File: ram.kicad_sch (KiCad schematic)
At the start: 7 parts, among them U1 LFE5U-85F-6BG381C, U2 IS42S16160J-6TL

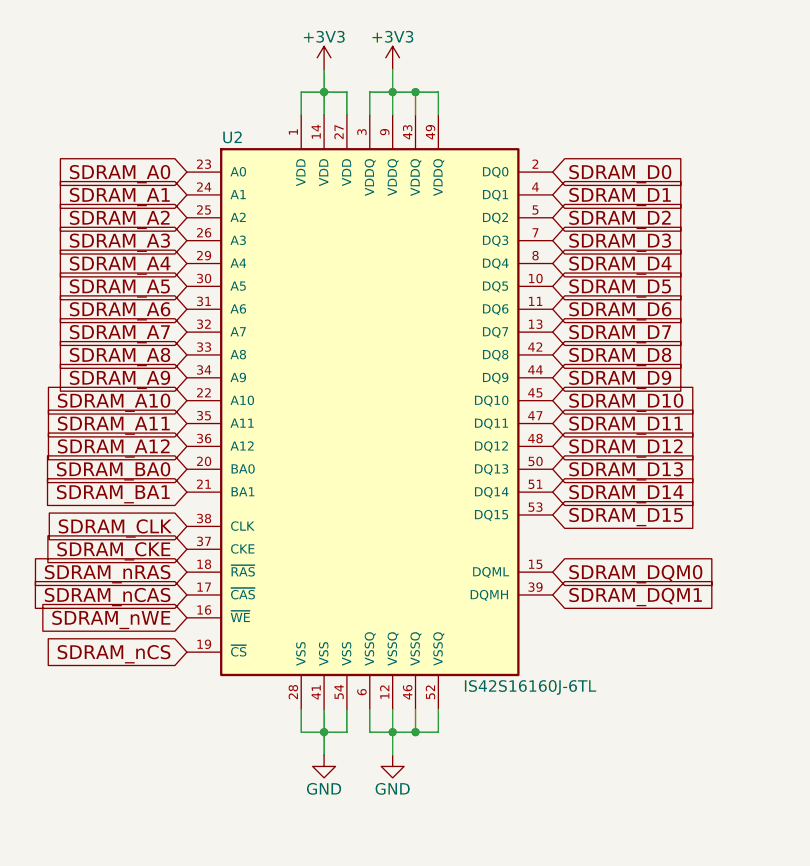
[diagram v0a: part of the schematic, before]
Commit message: update schematic with new footprint for ram. pre-wiring the ram on pcb
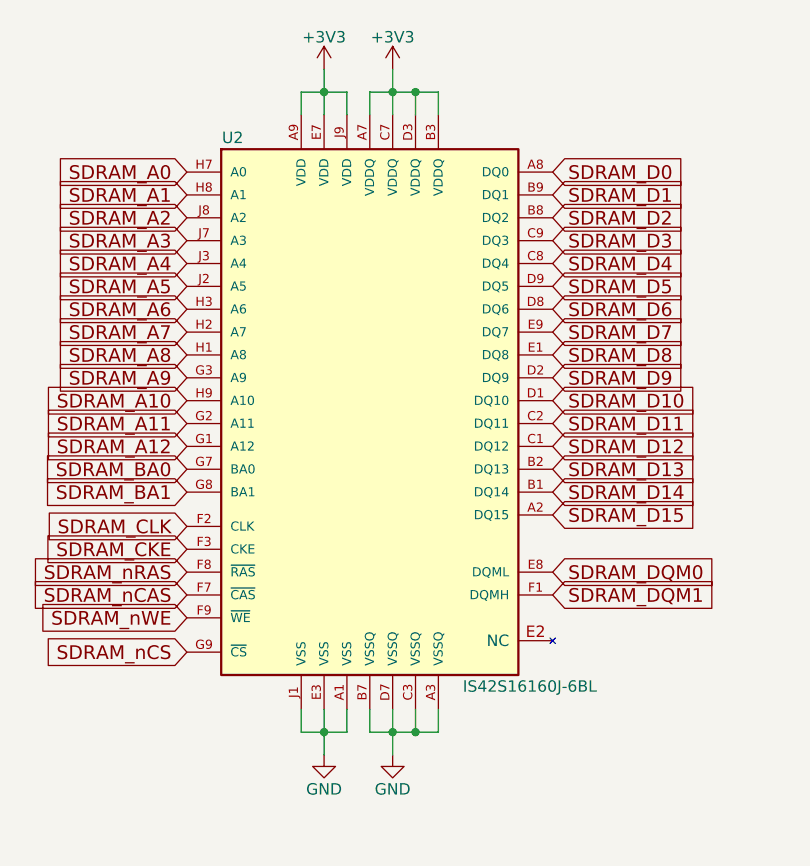
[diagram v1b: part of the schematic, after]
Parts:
- U2: value IS42S16160J-6TL -> IS42S16160J-6BL; footprint TSOP54:TSOP54 -> sdram:BGA54C80P9X9_800X800X120; symbol mt48lc16m16a2tg:MT48LC16M16A2TG -> mt48lc16m16a2tg:MT48LC16M16A2TG_BGA; MPN 870-IS42S16160J-6TL -> 870-42S16160J6BL
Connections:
- net +3V3: now also U2.A7 (VDDQ), U2.A9 (VDD), U2.B3 (VDDQ), U2.C7 (VDDQ), U2.D3 (VDDQ), U2.E7 (VDD), U2.J9 (VDD); no longer U2.1 (VDD), U2.14 (VDD), U2.27 (VDD), U2.3 (VDDQ), U2.43 (VDDQ), U2.49 (VDDQ), U2.9 (VDDQ)
- net GND: now also U2.A1 (VSS), U2.A3 (VSSQ), U2.B7 (VSSQ), U2.C3 (VSSQ), U2.D7 (VSSQ), U2.E3 (VSS), U2.J1 (VSS); no longer U2.12 (VSSQ), U2.28 (VSS), U2.41 (VSS), U2.46 (VSSQ), U2.52 (VSSQ), U2.54 (VSS), U2.6 (VSSQ)
- net SDRAM_A0: now also U2.H7 (A0); no longer U2.23 (A0)
- net SDRAM_A1: now also U2.H8 (A1); no longer U2.24 (A1)
- net SDRAM_A10: now also U2.H9 (A10); no longer U2.22 (A10)
- net SDRAM_A11: now also U2.G2 (A11); no longer U2.35 (A11)
- net SDRAM_A12: now also U2.G1 (A12); no longer U2.36 (A12)
- net SDRAM_A2: now also U2.J8 (A2); no longer U2.25 (A2)
- net SDRAM_A3: now also U2.J7 (A3); no longer U2.26 (A3)
- net SDRAM_A4: now also U2.J3 (A4); no longer U2.29 (A4)
- net SDRAM_A5: now also U2.J2 (A5); no longer U2.30 (A5)
- net SDRAM_A6: now also U2.H3 (A6); no longer U2.31 (A6)
- net SDRAM_A7: now also U2.H2 (A7); no longer U2.32 (A7)
- net SDRAM_A8: now also U2.H1 (A8); no longer U2.33 (A8)
- net SDRAM_A9: now also U2.G3 (A9); no longer U2.34 (A9)
- net SDRAM_BA0: now also U2.G7 (BA0); no longer U2.20 (BA0)
- net SDRAM_BA1: now also U2.G8 (BA1); no longer U2.21 (BA1)
- net SDRAM_CKE: now also U2.F3 (CKE); no longer U2.37 (CKE)
- net SDRAM_CLK: now also U2.F2 (CLK); no longer U2.38 (CLK)
- net SDRAM_D0: now also U2.A8 (DQ0); no longer U2.2 (DQ0)
- net SDRAM_D1: now also U2.B9 (DQ1); no longer U2.4 (DQ1)
- net SDRAM_D10: now also U2.D1 (DQ10); no longer U2.45 (DQ10)
- net SDRAM_D11: now also U2.C2 (DQ11); no longer U2.47 (DQ11)
- net SDRAM_D12: now also U2.C1 (DQ12); no longer U2.48 (DQ12)
- net SDRAM_D13: now also U2.B2 (DQ13); no longer U2.50 (DQ13)
- net SDRAM_D14: now also U2.B1 (DQ14); no longer U2.51 (DQ14)
- net SDRAM_D15: now also U2.A2 (DQ15); no longer U2.53 (DQ15)
- net SDRAM_D2: now also U2.B8 (DQ2); no longer U2.5 (DQ2)
- net SDRAM_D3: now also U2.C9 (DQ3); no longer U2.7 (DQ3)
- net SDRAM_D4: now also U2.C8 (DQ4); no longer U2.8 (DQ4)
- net SDRAM_D5: now also U2.D9 (DQ5); no longer U2.10 (DQ5)
- net SDRAM_D6: now also U2.D8 (DQ6); no longer U2.11 (DQ6)
- net SDRAM_D7: now also U2.E9 (DQ7); no longer U2.13 (DQ7)
- net SDRAM_D8: now also U2.E1 (DQ8); no longer U2.42 (DQ8)
- net SDRAM_D9: now also U2.D2 (DQ9); no longer U2.44 (DQ9)
- net SDRAM_DQM0: now also U2.E8 (DQML); no longer U2.15 (DQML)
- net SDRAM_DQM1: now also U2.F1 (DQMH); no longer U2.39 (DQMH)
- net SDRAM_nCAS: now also U2.F7 (~{CAS}); no longer U2.17 (~{CAS})
- net SDRAM_nCS: now also U2.G9 (~{CS}); no longer U2.19 (~{CS})
- net SDRAM_nRAS: now also U2.F8 (~{RAS}); no longer U2.18 (~{RAS})
- net SDRAM_nWE: now also U2.F9 (~{WE}); no longer U2.16 (~{WE})
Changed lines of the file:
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@@
 	)
 	(symbol
-		(lib_id "mt48lc16m16a2tg:MT48LC16M16A2TG")
+		(lib_id "mt48lc16m16a2tg:MT48LC16M16A2TG_BGA")
 		(at 138.43 88.9 0)
 		(unit 1)
@@
 			)
 		)
-		(property "Value" "IS42S16160J-6TL"
+		(property "Value" "IS42S16160J-6BL"
 			(at 156.21 119.38 0)
 			(show_name no)
@@
 			)
 		)
-		(property "Footprint" "TSOP54:TSOP54"
+		(property "Footprint" "sdram:BGA54C80P9X9_800X800X120"
 			(at 138.43 88.9 0)
 			(hide yes)
@@
 			)
 		)
-		(property "Description" ""
-			(at 138.43 88.9 0)
+		(property "Description" "SDRAM"
+			(at 138.43 88.9 0)
+			(hide yes)
 			(show_name no)
 			(do_not_autoplace no)
@@
 			)
 		)
-		(property "MPN" "870-IS42S16160J-6TL"
+		(property "MPN" "870-42S16160J6BL"
 			(at 138.43 88.9 0)
 			(hide yes)
@@
 			)
 		)
-		(pin "52"
-		)
-		(pin "2"
-		)
-		(pin "4"
-		)
-		(pin "5"
-		)
-		(pin "7"
-		)
-		(pin "8"
-		)
-		(pin "10"
-		)
-		(pin "11"
-		)
-		(pin "13"
-		)
-		(pin "42"
-		)
-		(pin "44"
-		)
-		(pin "45"
-		)
-		(pin "47"
-		)
-		(pin "48"
-		)
-		(pin "50"
-		)
-		(pin "51"
-		)
-		(pin "53"
-		)
-		(pin "15"
-		)
-		(pin "39"
-		)
-		(pin "23"
-		)
-		(pin "24"
-		)
-		(pin "25"
-		)
-		(pin "26"
-		)
-		(pin "29"
-		)
-		(pin "30"
-		)
-		(pin "31"
-		)
-		(pin "32"
-		)
-		(pin "33"
-		)
-		(pin "34"
-		)
-		(pin "22"
-		)
-		(pin "35"
-		)
-		(pin "36"
-		)
-		(pin "20"
-		)
-		(pin "21"
-		)
-		(pin "38"
-		)
-		(pin "37"
-		)
-		(pin "18"
-		)
-		(pin "17"
-		)
-		(pin "16"
-		)
-		(pin "19"
-		)
-		(pin "1"
-		)
-		(pin "28"
-		)
-		(pin "14"
-		)
-		(pin "41"
-		)
-		(pin "27"
-		)
-		(pin "54"
-		)
-		(pin "3"
-		)
-		(pin "6"
-		)
-		(pin "9"
-		)
-		(pin "12"
-		)
-		(pin "43"
-		)
-		(pin "46"
-		)
-		(pin "49"
+		(pin "F3"
+		)
+		(pin "F2"
+		)
+		(pin "D2"
+		)
+		(pin "J8"
+		)
+		(pin "C9"
+		)
+		(pin "A2"
+		)
+		(pin "J3"
+		)
+		(pin "C7"
+		)
+		(pin "B1"
+		)
+		(pin "J2"
+		)
+		(pin "H7"
+		)
+		(pin "D9"
+		)
+		(pin "D7"
+		)
+		(pin "B2"
+		)
+		(pin "A1"
+		)
+		(pin "G9"
+		)
+		(pin "A7"
+		)
+		(pin "G3"
+		)
+		(pin "H8"
+		)
+		(pin "E2"
+		)
+		(pin "H2"
+		)
+		(pin "D3"
+		)
+		(pin "B9"
+		)
+		(pin "B7"
+		)
+		(pin "E7"
+		)
+		(pin "G8"
+		)
+		(pin "A3"
+		)
+		(pin "F1"
+		)
+		(pin "D1"
+		)
+		(pin "H3"
+		)
+		(pin "E3"
+		)
+		(pin "C8"
+		)
+		(pin "C2"
+		)
+		(pin "E9"
+		)
+		(pin "J1"
+		)
+		(pin "F7"
+		)
+		(pin "C3"
+		)
+		(pin "A9"
+		)
+		(pin "H1"
+		)
+		(pin "B8"
+		)
+		(pin "C1"
+		)
+		(pin "G1"
+		)
+		(pin "E1"
+		)
+		(pin "D8"
+		)
+		(pin "B3"
+		)
+		(pin "J9"
+		)
+		(pin "G7"
+		)
+		(pin "F8"
+		)
+		(pin "G2"
+		)
+		(pin "H9"
+		)
+		(pin "E8"
+		)
+		(pin "A8"
+		)
+		(pin "F9"
+		)
+		(pin "J7"
 		)
 		(instances

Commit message: replaced psu, need to still to drc
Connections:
- no-connect marks 11 -> 10
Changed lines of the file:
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@@
-	)
-	(no_connect
-		(at 184.15 144.78)
 	)
 	(no_connect

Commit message: update parts for 22uf/1uf. Update footprint for RP* items
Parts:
- U2: Digikey (none) -> IS42S16160J-6BL-ND

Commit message: done with routing
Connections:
- no-connect marks 10 -> 12
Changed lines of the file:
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@@
+	)
+	(no_connect
+		(at 217.17 97.79)
+	)
+	(no_connect
+		(at 255.27 97.79)
 	)
 	(no_connect
